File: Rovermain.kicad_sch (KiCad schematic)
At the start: 59 parts, among them J1 48V input, J10 3V3 Output, J11 5V Output, J12 Pi_48V_Control, J13 Steering Bus Bar, J14 Drive Bus Bar, J15 Arm Bus Bar, J17 Spare 48V port, J2 USB_C_Receptacle_Pi_Power, J3 24V Output, J4 USB_C_Receptacle_Spare_power, J5 Buck 48/24, J6 Buck 24/12, J7 Buck 24/5, J8 Buck 12/3V3, J9 12V Output, Q1 Arm ctrl, Q2 Steer ctrl, Q3 Drive ctrl, Q4 Spare ctrl, SW2 SW_Push_Open

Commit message: more routing; added fuses
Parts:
- added F11, F12, F13, F14: Fuse, Fuse:Fuse_0603_1608Metric, symbol Device:Fuse
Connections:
- net 48V: now also F11.1, F12.1, F13.1, F14.1; no longer D10.1 (K), D11.1 (K), D12.1 (K), D9.1 (K)
- new net: D9.1 (K), F12.2
- new net: D12.1 (K), F14.2
- new net: D11.1 (K), F11.2
- new net: D10.1 (K), F13.2

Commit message: updated usb-c ports; finalized routing
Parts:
- J2, J4: footprint USB-C-PD-2171750001:2171750001_MOL -> Real_USB-C-PD-2171750001:2171750001_MOL
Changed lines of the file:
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@@
 			)
 		)
-		(property "Footprint" "USB-C-PD-2171750001:2171750001_MOL"
+		(property "Footprint" "Real_USB-C-PD-2171750001:2171750001_MOL"
 			(at 93.98 38.1 0)
 			(hide yes)
@@
 			)
 		)
-		(property "Footprint" "USB-C-PD-2171750001:2171750001_MOL"
+		(property "Footprint" "Real_USB-C-PD-2171750001:2171750001_MOL"
 			(at 38.1 36.83 0)
 			(hide yes)

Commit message: removed high amperage lines, populated 3D model, added mounting
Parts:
- removed D10, D11, D12, D9: D, SM74611KTTR:TO254P1524X483-3N, symbol Device:D
- removed F11, F12, F13, F14, F6: Fuse, Fuse:Fuse_0603_1608Metric, symbol Device:Fuse
- removed J12: Pi_48V_Control, TerminalBlock_Phoenix:TerminalBlock_Phoenix_PT-1,5-4-5.0-H_1x04_P5.00mm_Horizontal, symbol Connector_Generic:Conn_01x04
- removed J13: Steering Bus Bar, TerminalBlock_Phoenix:TerminalBlock_Phoenix_PT-1,5-2-5.0-H_1x02_P5.00mm_Horizontal, symbol Connector_Generic:Conn_01x02
- removed J14: Drive Bus Bar, TerminalBlock_Phoenix:TerminalBlock_Phoenix_PT-1,5-2-5.0-H_1x02_P5.00mm_Horizontal, symbol Connector_Generic:Conn_01x02
- removed J15: Arm Bus Bar, TerminalBlock_Phoenix:TerminalBlock_Phoenix_PT-1,5-2-5.0-H_1x02_P5.00mm_Horizontal, symbol Connector_Generic:Conn_01x02
- removed J17: Spare 48V port, TerminalBlock_Phoenix:TerminalBlock_Phoenix_PT-1,5-2-5.0-H_1x02_P5.00mm_Horizontal, symbol Connector_Generic:Conn_01x02
- removed Q1: Arm ctrl, Package_TO_SOT_SMD:TDSON-8-1, symbol Transistor_FET:FDMS86150ET100
- removed Q2: Steer ctrl, Package_TO_SOT_SMD:TDSON-8-1, symbol Transistor_FET:FDMS86150ET100
- removed Q3: Drive ctrl, Package_TO_SOT_SMD:TDSON-8-1, symbol Transistor_FET:FDMS86150ET100
- removed Q4: Spare ctrl, Package_TO_SOT_SMD:TDSON-8-1, symbol Transistor_FET:FDMS86150ET100
- removed R12, R13, R14, R19: 100kohm, Resistor_SMD:R_0402_1005Metric, symbol Device:R
- removed R15, R16, R17, R18: 100ohm, Resistor_SMD:R_1206_3216Metric, symbol Device:R
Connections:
- net at J1.2 (Pin_2): now also RL1.14

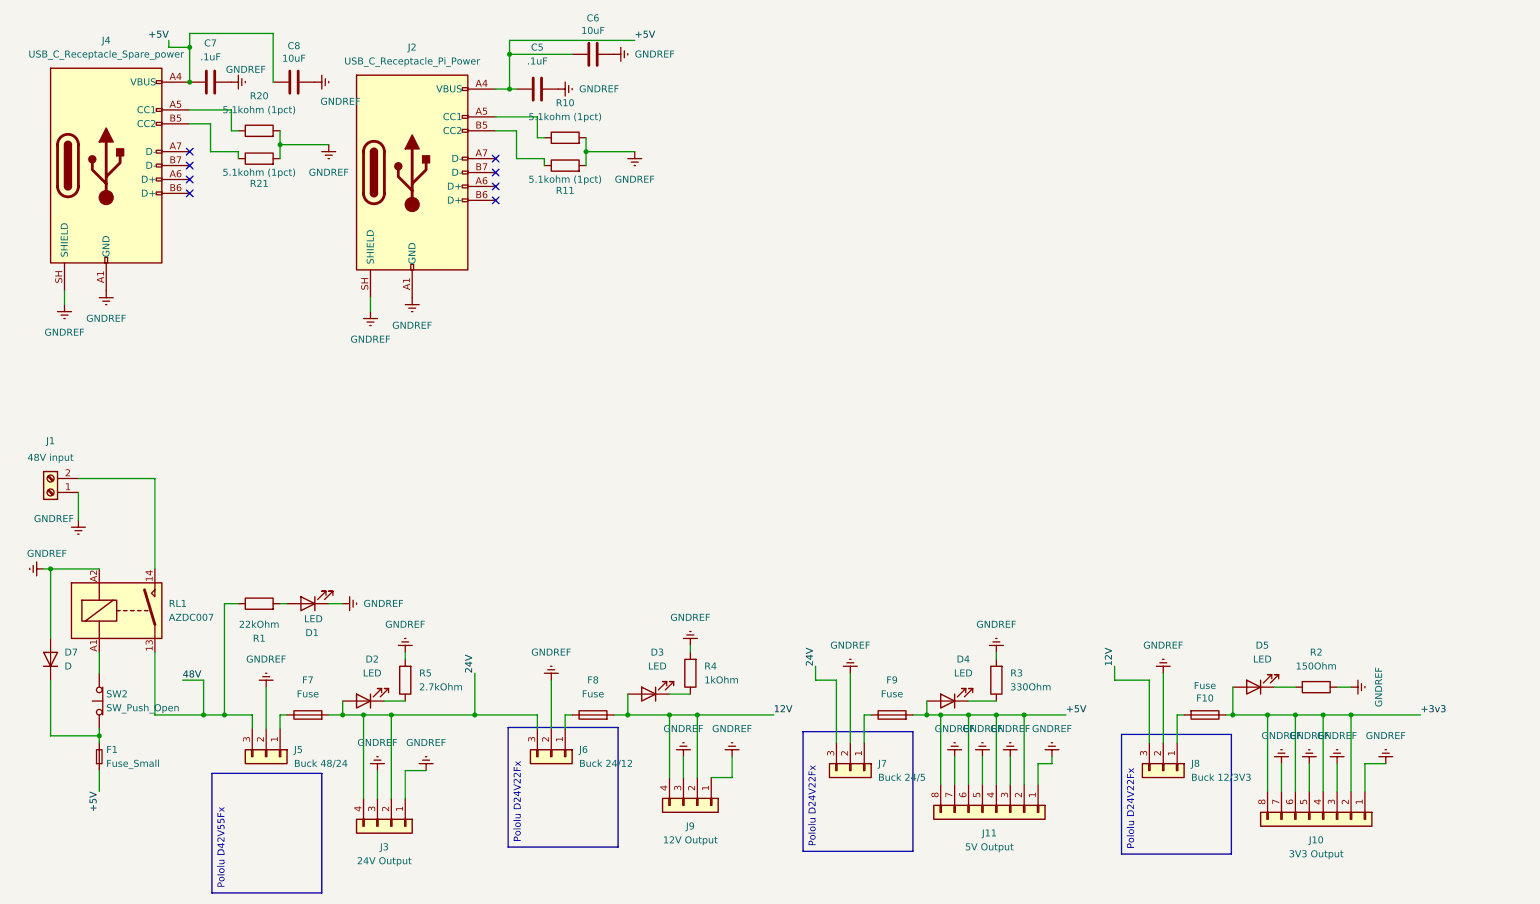
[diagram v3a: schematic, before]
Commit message: added CAN support; labels
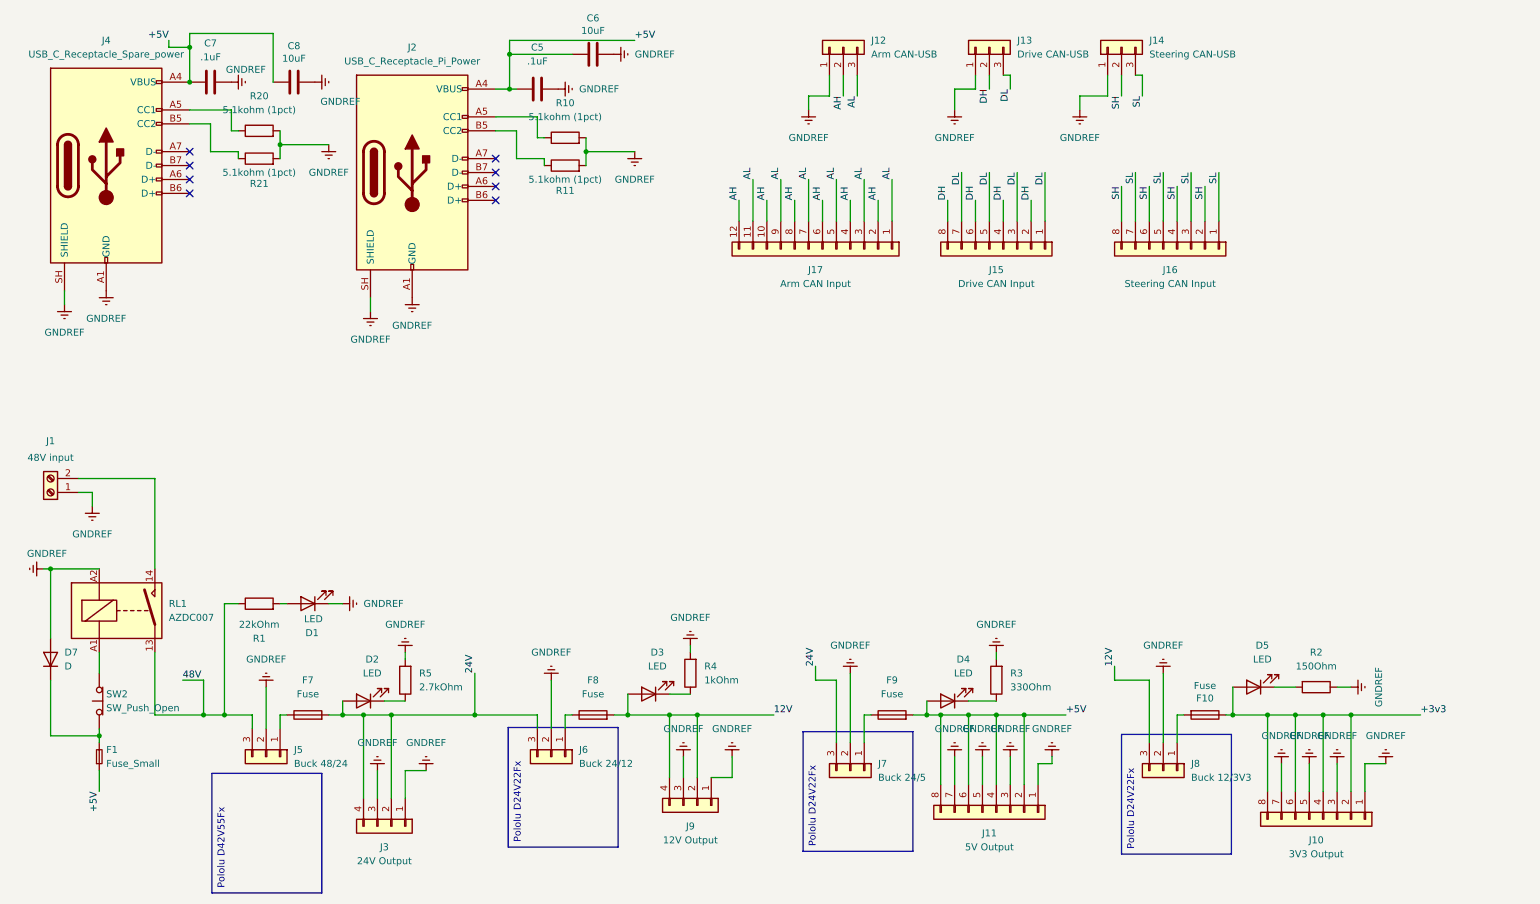
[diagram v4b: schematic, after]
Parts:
- added J12: Arm CAN-USB, TerminalBlock_Phoenix:TerminalBlock_Phoenix_PT-1,5-3-5.0-H_1x03_P5.00mm_Horizontal, symbol Connector_Generic:Conn_01x03
- added J13: Drive CAN-USB, TerminalBlock_Phoenix:TerminalBlock_Phoenix_PT-1,5-3-5.0-H_1x03_P5.00mm_Horizontal, symbol Connector_Generic:Conn_01x03
- added J14: Steering CAN-USB, TerminalBlock_Phoenix:TerminalBlock_Phoenix_PT-1,5-3-5.0-H_1x03_P5.00mm_Horizontal, symbol Connector_Generic:Conn_01x03
- added J15: Drive CAN Input, TerminalBlock_Phoenix:TerminalBlock_Phoenix_PT-1,5-8-5.0-H_1x08_P5.00mm_Horizontal, symbol Connector_Generic:Conn_01x08
- added J16: Steering CAN Input, TerminalBlock_Phoenix:TerminalBlock_Phoenix_PT-1,5-8-5.0-H_1x08_P5.00mm_Horizontal, symbol Connector_Generic:Conn_01x08
- added J17: Arm CAN Input, TerminalBlock_Phoenix:TerminalBlock_Phoenix_PT-1,5-12-5.0-H_1x12_P5.00mm_Horizontal, symbol Connector_Generic:Conn_01x12
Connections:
- net GNDREF: now also J12.1 (Pin_1), J13.1 (Pin_1), J14.1 (Pin_1)
- new net AH: J12.2 (Pin_2), J17.10 (Pin_10), J17.12 (Pin_12), J17.2 (Pin_2), J17.4 (Pin_4), J17.6 (Pin_6), J17.8 (Pin_8)
- new net AL: J12.3 (Pin_3), J17.1 (Pin_1), J17.11 (Pin_11), J17.3 (Pin_3), J17.5 (Pin_5), J17.7 (Pin_7), J17.9 (Pin_9)
- new net DH: J13.2 (Pin_2), J15.2 (Pin_2), J15.4 (Pin_4), J15.6 (Pin_6), J15.8 (Pin_8)
- new net DL: J13.3 (Pin_3), J15.1 (Pin_1), J15.3 (Pin_3), J15.5 (Pin_5), J15.7 (Pin_7)
- new net SH: J14.2 (Pin_2), J16.2 (Pin_2), J16.4 (Pin_4), J16.6 (Pin_6), J16.8 (Pin_8)
- new net SL: J14.3 (Pin_3), J16.1 (Pin_1), J16.3 (Pin_3), J16.5 (Pin_5), J16.7 (Pin_7)

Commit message: schematic overhaul for CAN2USB
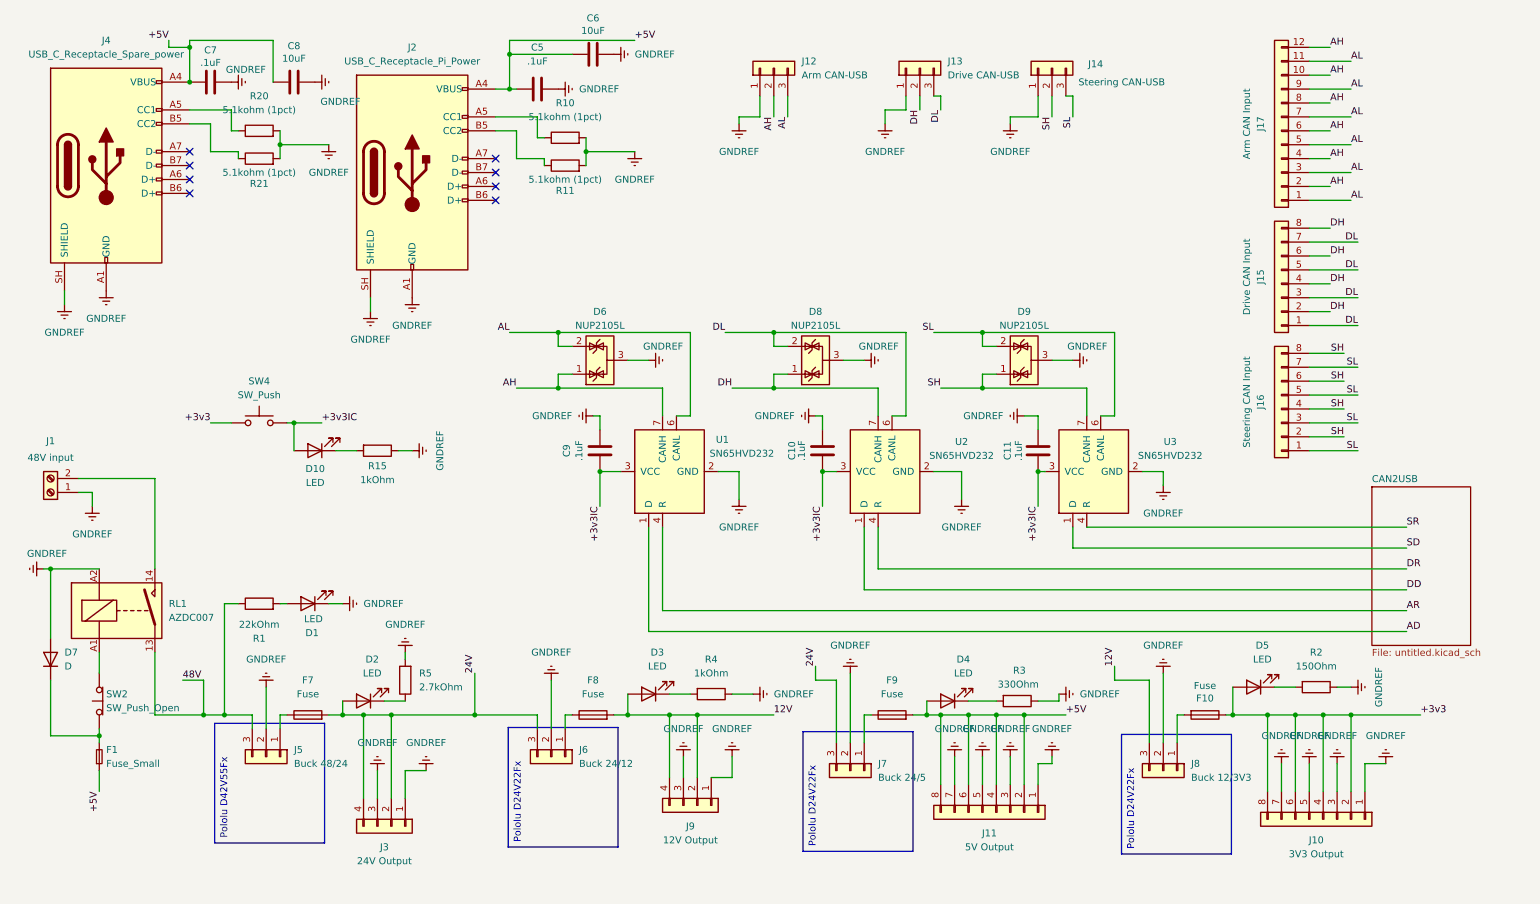
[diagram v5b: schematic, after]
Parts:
- added C10, C11, C9: .1uF, Capacitor_SMD:C_0603_1608Metric, symbol Device:C
- added D10: LED, LED_SMD:LED_0603_1608Metric, symbol Device:LED
- added D6, D8, D9: NUP2105L, Package_TO_SOT_SMD:SOT-23, symbol Power_Protection:NUP2105L
- added R15: 1kOhm, Resistor_SMD:R_1206_3216Metric, symbol Device:R
- added SW4: SW_Push, Package_DIP:DIP-24_W7.62mm, symbol Switch:SW_Push
- added U1, U2, U3: SN65HVD232, Package_SO:SOIC-8_3.9x4.9mm_P1.27mm, symbol Interface_CAN_LIN:SN65HVD232
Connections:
- net +3v3: now also SW4.1
- net AH: now also D6.1 (K), U1.7 (CANH)
- net AL: now also D6.2 (K), U1.6 (CANL)
- net DH: now also D8.1 (K), U2.7 (CANH)
- net DL: now also D8.2 (K), U2.6 (CANL)
- net GNDREF: now also R3.1, R4.1, C10.2, C11.2, C9.2, D6.3 (A), D8.3 (A), D9.3 (A), R15.1, U1.2 (GND), U2.2 (GND), U3.2 (GND); no longer R3.2, R4.2
- net SH: now also D9.1 (K), U3.7 (CANH)
- net SL: now also D9.2 (K), U3.6 (CANL)
- net at D3.1 (K): now also R4.2; no longer R4.1
- net at D4.1 (K): now also R3.2; no longer R3.1
- new net: D10.1 (K), R15.2
- new net +3v3IC: C10.1, C11.1, C9.1, D10.2 (A), SW4.2, U1.3 (VCC), U2.3 (VCC), U3.3 (VCC)
- new net AD: U1.1 (D)
- new net AR: U1.4 (R)
- new net DD: U2.1 (D)
- new net DR: U2.4 (R)
- new net SD: U3.1 (D)
- new net SR: U3.4 (R)
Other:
- added sheet CAN2USB (untitled.kicad_sch)
- moved on the sheet: J12, J13, J14, J15, J16, J17, R3, R4

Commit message: big routing
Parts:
- added R27, R28, R29: 120Ohm, Resistor_SMD:R_0603_1608Metric, symbol Device:R
- SW4: value SW_Push -> CAN2USB_Enable; footprint Package_DIP:DIP-24_W7.62mm -> Button-GPTS2032:SWITCH_03211B
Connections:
- net AH: now also R27.1
- net AL: now also R27.2
- net DH: now also R28.1
- net DL: now also R28.2
- net SH: now also R29.1
- net SL: now also R29.2
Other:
- moved on the sheet: D10, R15, SW4
